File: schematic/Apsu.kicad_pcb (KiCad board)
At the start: 2 copper layers, 76.7 x 52.7 mm, 79 parts, among them J1 Conn_02x03_Odd_Even, J10 Conn_01x03, J11 Conn_01x03, J12 Conn_01x02_Male, J13 Conn_01x02, J14 Conn_01x11_Male, J15 Conn_01x03_Female, J2 Conn_02x05_Odd_Even, J3 Conn_02x06_Odd_Even, J4 Conn_01x05, J5 Conn_01x05, J6 Conn_01x03, J7 Conn_01x02, J8 Conn_01x03_Female, J9 Conn_01x03, U1 ESP32-WROOM-32, U10 MAX6682MUA+T, U2 PCA9685PW, U3 ADS1015IDGS, U4 FAN4860UC5X, U5 LIS2MDL, U6 LSM6DSOX, U7 BME280, U8 SP3485CN, U9 MC74HC138A

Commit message: wireing
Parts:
- C10, C12, C13, C9, U5: moved to B.Cu
- moved C14 30.3 mm to (121.5, 112.0)
- moved C11 29.0 mm to (125.5, 109.5), turned to 270 degrees
- moved U6 24.0 mm to (125.0, 113.5), turned to 180 degrees
- moved C10 7.96 mm to (176.2, 120.6), turned to 180 degrees
- moved C13 7.02 mm to (169.5, 121.5), turned to 180 degrees
- moved C12 6.52 mm to (169.5, 119.5)
- moved C6 1.91 mm to (164.8, 101.4)
- moved C9 1.58 mm to (169.5, 123.5)
- moved J1 1.45 mm to (121.0, 104.0)
- moved J14 1.00 mm to (165.7, 122.5)
- moved U5 0.71 mm to (173.5, 123.0), turned to 90 degrees
- moved C7 0.50 mm to (158.0, 112.0)
- moved C8 0.50 mm to (153.0, 112.0)
- moved U3 0.50 mm to (168.0, 101.0)
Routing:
- net GND: track 0.00 -> 523.8 mm, vias 0 -> 6
- net +3V3: track 0.00 -> 381.5 mm, vias 0 -> 6
- net I2C-SCL: track 0.00 -> 161.6 mm, vias 0 -> 6
- net I2C-SDA: track 0.00 -> 160.5 mm, vias 0 -> 6
- net RS485-A: track 0.00 -> 83.5 mm
- net SPI-SCLK: track 0.00 -> 79.1 mm, vias 0 -> 5
- net JTAG-TDO: track 0.00 -> 75.7 mm, vias 0 -> 2
- net RS485-B: track 0.00 -> 72.0 mm, vias 0 -> 1
- net SPI-MISO: track 0.00 -> 68.3 mm, vias 0 -> 2
- net ESP_RXD: track 0.00 -> 66.9 mm, vias 0 -> 2
- net DS18B20: track 0.00 -> 66.7 mm, vias 0 -> 2
- net ESP_TXD: track 0.00 -> 64.0 mm, vias 0 -> 2
- net SPI-SS2: track 0.00 -> 63.0 mm, vias 0 -> 3
- net SPI-SS0: track 0.00 -> 62.9 mm, vias 0 -> 1
- net SPI-SS1: track 0.00 -> 56.7 mm, vias 0 -> 1
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- added copper zone on B.Cu, net GND
- added copper zone on F.Cu, net GND
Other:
- net class JLCPCB added: clearance 0.127, trace_width 0.127, via_dia 0.45, via_drill 0.2
- net class midden added: clearance 0.2, trace_width 0.2, via_dia 0.5, via_drill 0.3
- rule trace_min: 0.2 -> 0.127
- rule via_min_drill: 0.3 -> 0.2
- rule via_min_size: 0.4 -> 0.45

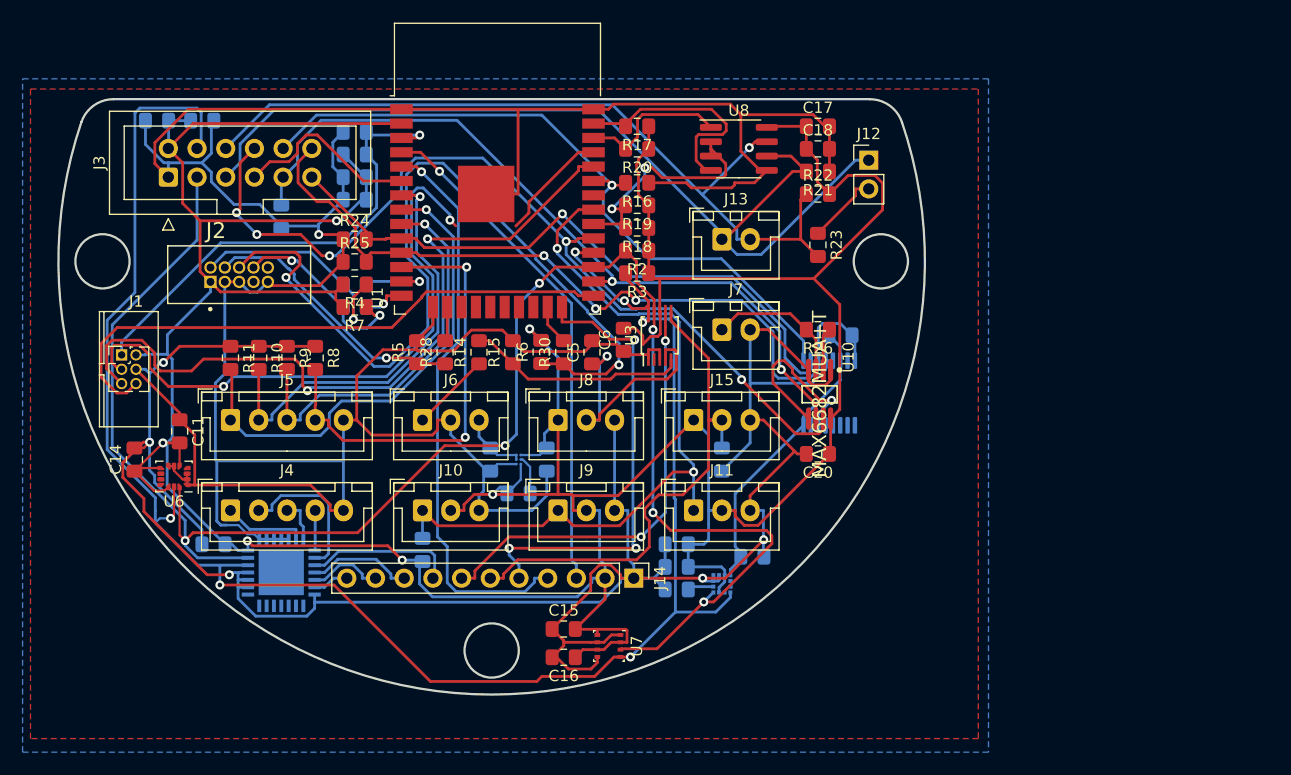
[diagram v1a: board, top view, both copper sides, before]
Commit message: on-pcb documentation
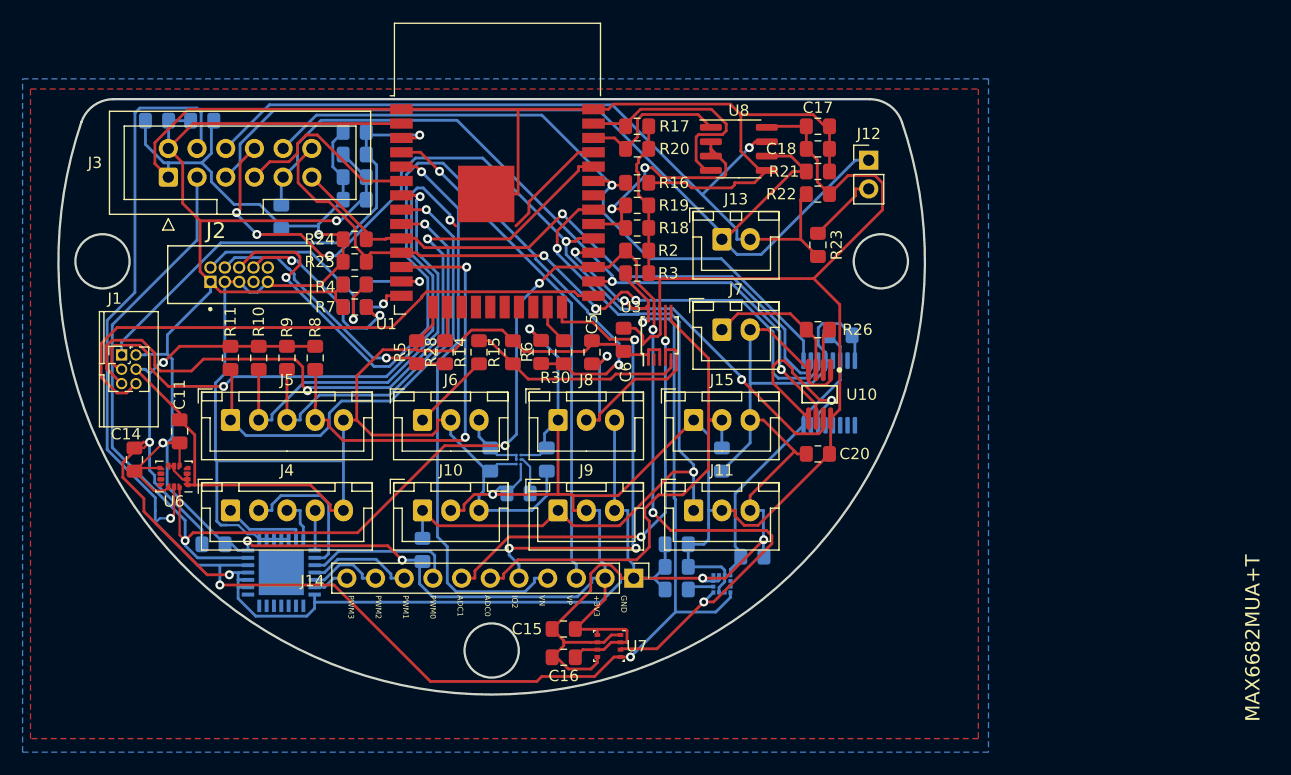
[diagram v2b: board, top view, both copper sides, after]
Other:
- board text added: "+3V3 GND BOOT"
- board text added: "+5V GND press"
- board text added: "Aruna - Apsu github.com/aruna-rov/Apsu"
- board text added: "EN TX RX"
- board text added: "GND +3V3 DS18B20"
- board text added: "GND +3V3 VP VN IO2 ADC0 ADC1 PWM0 PWM1 PWM2 PWM3"
- board text added: "GND M3 M1 M4 M2"
- board text added: "GND NC GND GND +3V3"
- board text added: "GND TL TR BL BR"
- board text added: "GND Therm"
- board text added: "GND w0 +3V3"
- board text added: "GND w1 +3V3"
- board text added: "NC TDI TDO TCK TMS"
- board text added: "RS485 120R"
- board text added: "RS485-B RS485-A"
- board text added: "SPI-SS1 SPI-MISO SPI-MOSI RS485-A I²C-SDA GND"
- board text added: "SPI-SS2 SPI-SS0 SPI-SCLK RS485-B I²C-SCL +3V3"

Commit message: added version
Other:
- board text added: "Aruna - Apsu github.com/aruna-rov/Apsu V1"
- board text removed: "Aruna - Apsu github.com/aruna-rov/Apsu"

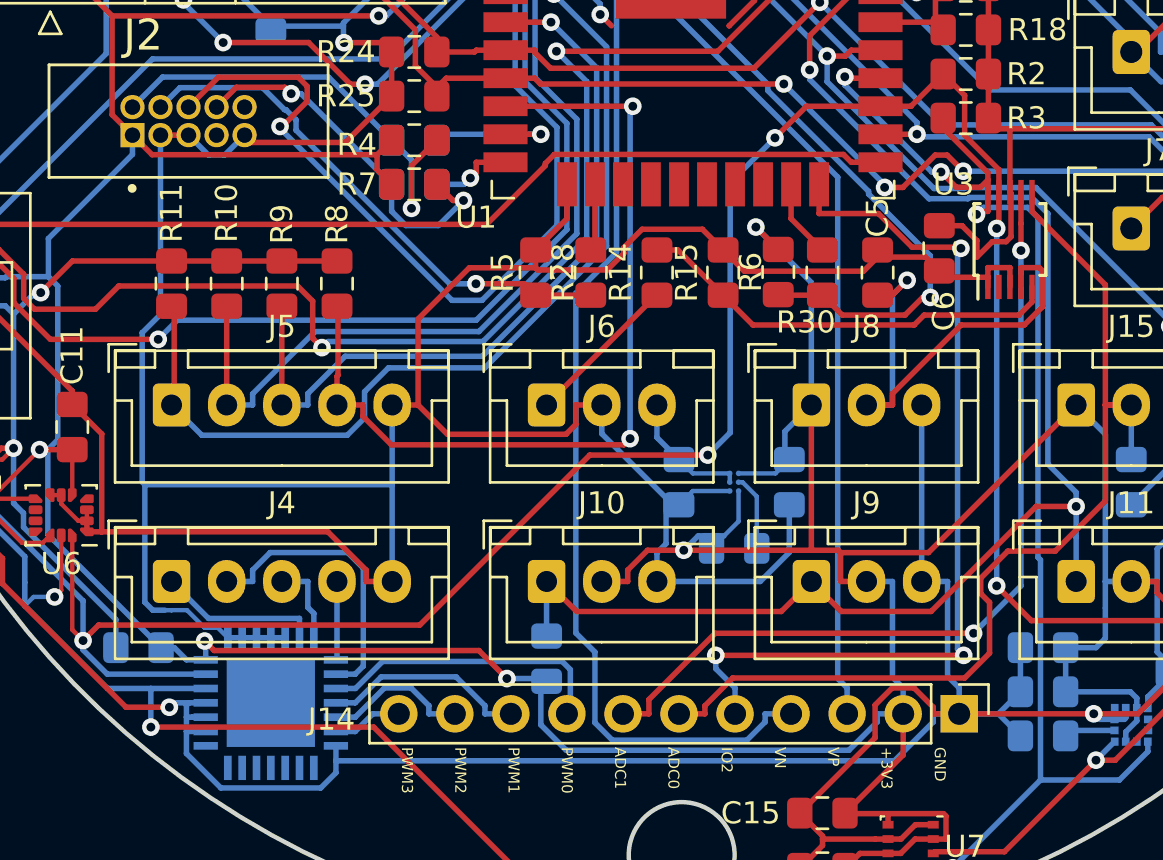
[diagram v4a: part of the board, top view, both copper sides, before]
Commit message: added MPN
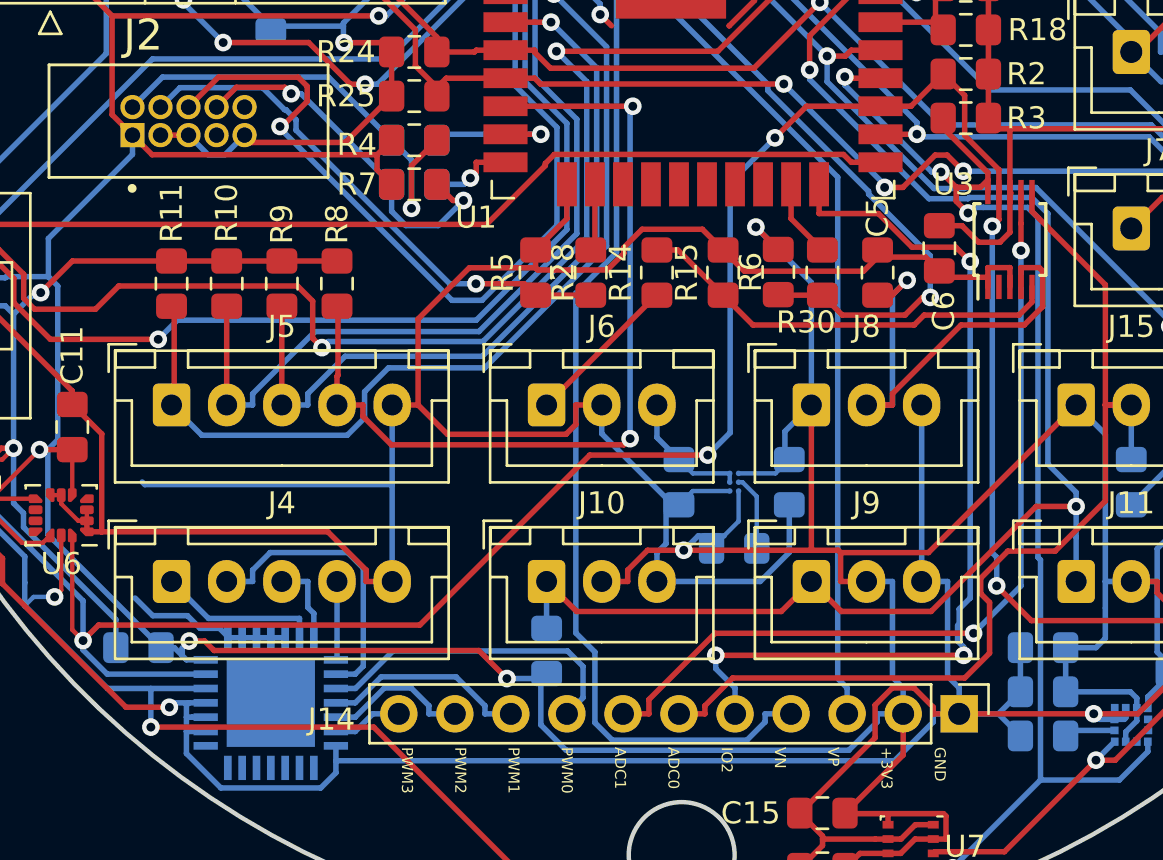
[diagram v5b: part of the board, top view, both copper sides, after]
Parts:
- moved R13 0.35 mm to (147.0, 119.7)
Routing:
- net GND: track 523.8 -> 502.9 mm
- net PWM_custom_0: track 13.4 -> 14.9 mm
